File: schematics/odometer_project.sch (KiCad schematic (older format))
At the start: 8 parts, among them J2 Conn_01x03_Female, J3 Conn_02x10_Odd_Even, J4 Conn_02x10_Odd_Even, U1 SN74HC14N

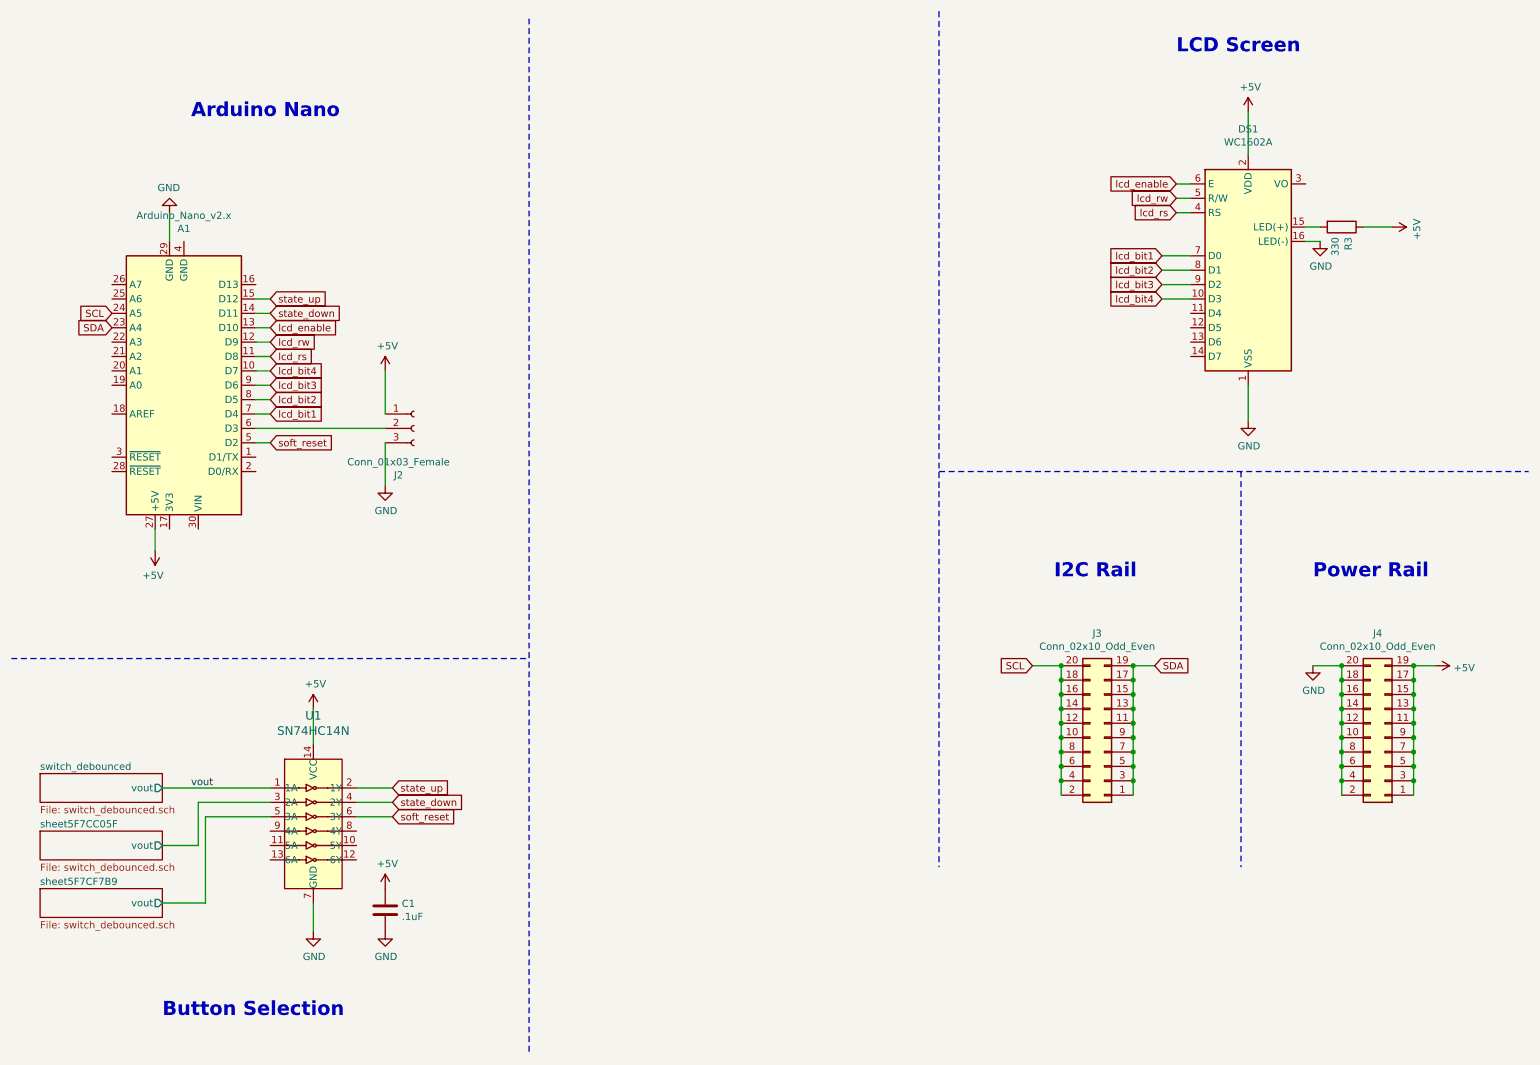
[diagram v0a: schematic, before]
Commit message: fixed lcd pin connections and xtra halls
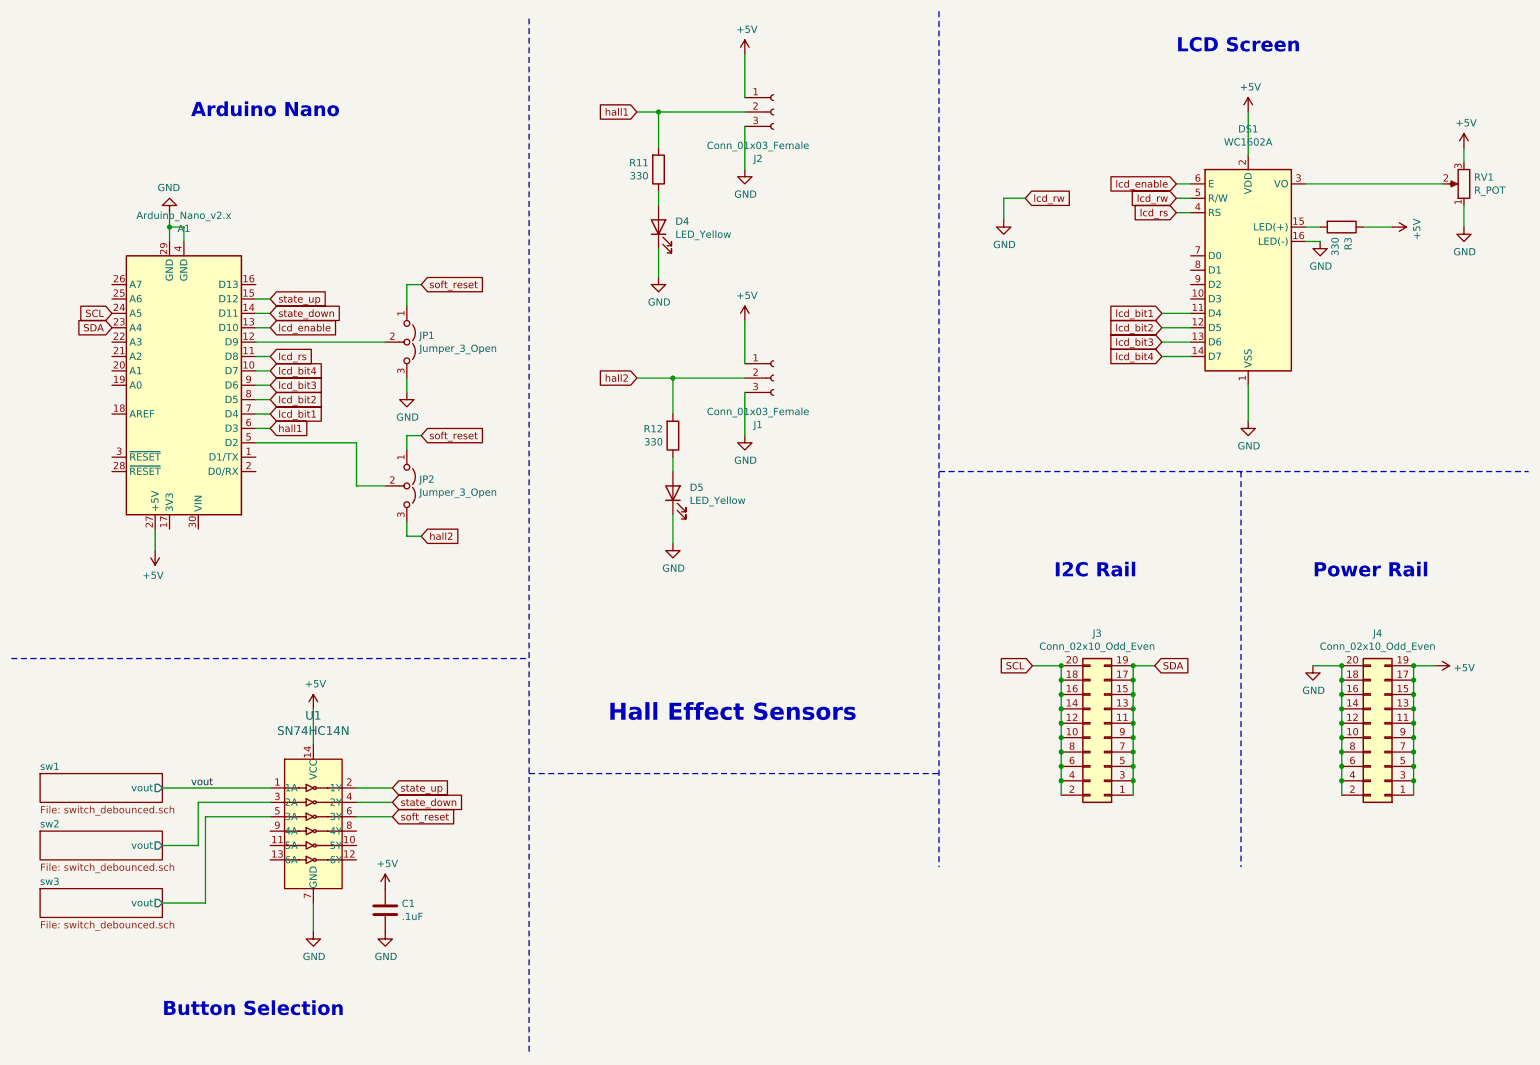
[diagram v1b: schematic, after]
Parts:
- added D4, D5: LED_Yellow, LED_SMD:LED_0805_2012Metric_Pad1.15x1.40mm_HandSolder, symbol Device:LED
- added J1: Conn_01x03_Female, Connector_PinHeader_2.54mm:PinHeader_1x03_P2.54mm_Horizontal, symbol Connector:Conn_01x03_Female
- added JP1, JP2: Jumper_3_Open, Connector_PinHeader_2.54mm:PinHeader_1x03_P2.54mm_Vertical, symbol Jumper:Jumper_3_Open
- added R11, R12: 330, Resistor_SMD:R_0805_2012Metric_Pad1.15x1.40mm_HandSolder, symbol Device:R
- added RV1: R_POT, Potentiometer_THT:Potentiometer_Bourns_3296W_Vertical, symbol Device:R_POT
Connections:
- net +5V: now also J1.1 (Pin_1), RV1.3
- net GND: now also A1.4 (GND), DS1.5 (R/W), D4.1 (K), D5.1 (K), J1.3 (Pin_3), JP1.3 (B), RV1.1
- net lcd_bit1: now also DS1.11 (D4); no longer DS1.7 (D0)
- net lcd_bit2: now also DS1.12 (D5); no longer DS1.8 (D1)
- net lcd_bit3: now also DS1.13 (D6); no longer DS1.9 (D2)
- net lcd_bit4: now also DS1.14 (D7); no longer DS1.10 (D3)
- net soft_reset: now also JP1.1 (A), JP2.1 (A); no longer A1.5 (D2)
- net hall1: now reaches A1.6 (D3), J2.2 (Pin_2)
- net hall1: now also R11.2
- net at DS1.3 (VO): now also RV1.2
- net lcd_rw: no longer names the net of A1.12 (D9)
- net lcd_rw: now also JP1.2 (C); no longer DS1.5 (R/W)
- net sheet5F7CC05F/vout renamed sw2/vout
- net sheet5F7CF7B9/vout renamed sw3/vout
- new net: A1.5 (D2), JP2.2 (C)
- new net: D4.2 (A), R11.1
- new net: D5.2 (A), R12.1
- new net hall2: J1.2 (Pin_2), JP2.3 (B), R12.2
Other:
- note added: "Hall Effect Sensors"
- moved on the sheet: J2

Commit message: added schematic notes
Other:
- note added: "Don't stress about these jumpers.\nJust connect a line straight from soft_reset"
- note added: "dont worry about the\nsecond hall effect sensor"
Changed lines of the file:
@@
 Rev "2.1"
 Comp "DES Gang"
-Comment1 "refer to referenced sheets where nessesary"
-Comment2 ""
+Comment1 "just use buttons and pull down resistors for the butotn selection - dw bout debouncing just yet..."
+Comment2 "dont worry about attaching a second hall effect for now"
 Comment3 ""
 Comment4 ""
@@
 Text GLabel 8700 1700 0    50   Input ~ 0
 lcd_enable
-Text GLabel 8700 1800 0    50   Input ~ 0
-lcd_rw
 Text GLabel 8700 1900 0    50   Input ~ 0
 lcd_rs
@@
 Wire Wire Line
 	8700 1900 8800 1900
-Wire Wire Line
-	8800 1800 8700 1800
 Wire Wire Line
 	9600 2000 9700 2000
@@
 Wire Wire Line
 	5200 3050 5700 3050
-Text GLabel 7650 1800 2    50   Input ~ 0
-lcd_rw
-Wire Wire Line
-	7650 1800 7500 1800
-Wire Wire Line
-	7500 1800 7500 1950
-$Comp
-L power:GND #PWR0121
-U 1 1 5F875B74
-P 7500 1950
-F 0 "#PWR0121" H 7500 1700 50  0001 C CNN
-F 1 "GND" H 7505 1777 50  0000 C CNN
-F 2 "" H 7500 1950 50  0001 C CNN
-F 3 "" H 7500 1950 50  0001 C CNN
-	1    7500 1950
-	1    0    0    -1
-$EndComp
 $Comp
 L Device:R_POT RV1
@@
 Wire Wire Line
 	1700 2000 1700 1900
+Text Notes 2200 4550 0    50   ~ 10
+Don't stress about these jumpers.\nJust connect a line straight from soft_reset
+Text Notes 5600 4250 0    50   ~ 10
+dont worry about the\nsecond hall effect sensor
+Wire Wire Line
+	8300 1800 8300 1950
+$Comp
+L power:GND #PWR0121
+U 1 1 5F875B74
+P 8300 1950
+F 0 "#PWR0121" H 8300 1700 50  0001 C CNN
+F 1 "GND" H 8305 1777 50  0000 C CNN
+F 2 "" H 8300 1950 50  0001 C CNN
+F 3 "" H 8300 1950 50  0001 C CNN
+	1    8300 1950
+	1    0    0    -1
+$EndComp
+Wire Wire Line
+	8300 1800 8800 1800
 $EndSCHEMATC
